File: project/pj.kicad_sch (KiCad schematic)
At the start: 15 parts, among them J1 RPi_GPIO, J10 Pico PWR enable, J2 2B+, J3 zero, J4 3A+, J5 3B+, J6 4, J7 Conn_01x02, J8 Conn_01x02, J9 External PWR, SW1 SW_Push, SW2 SW_Push

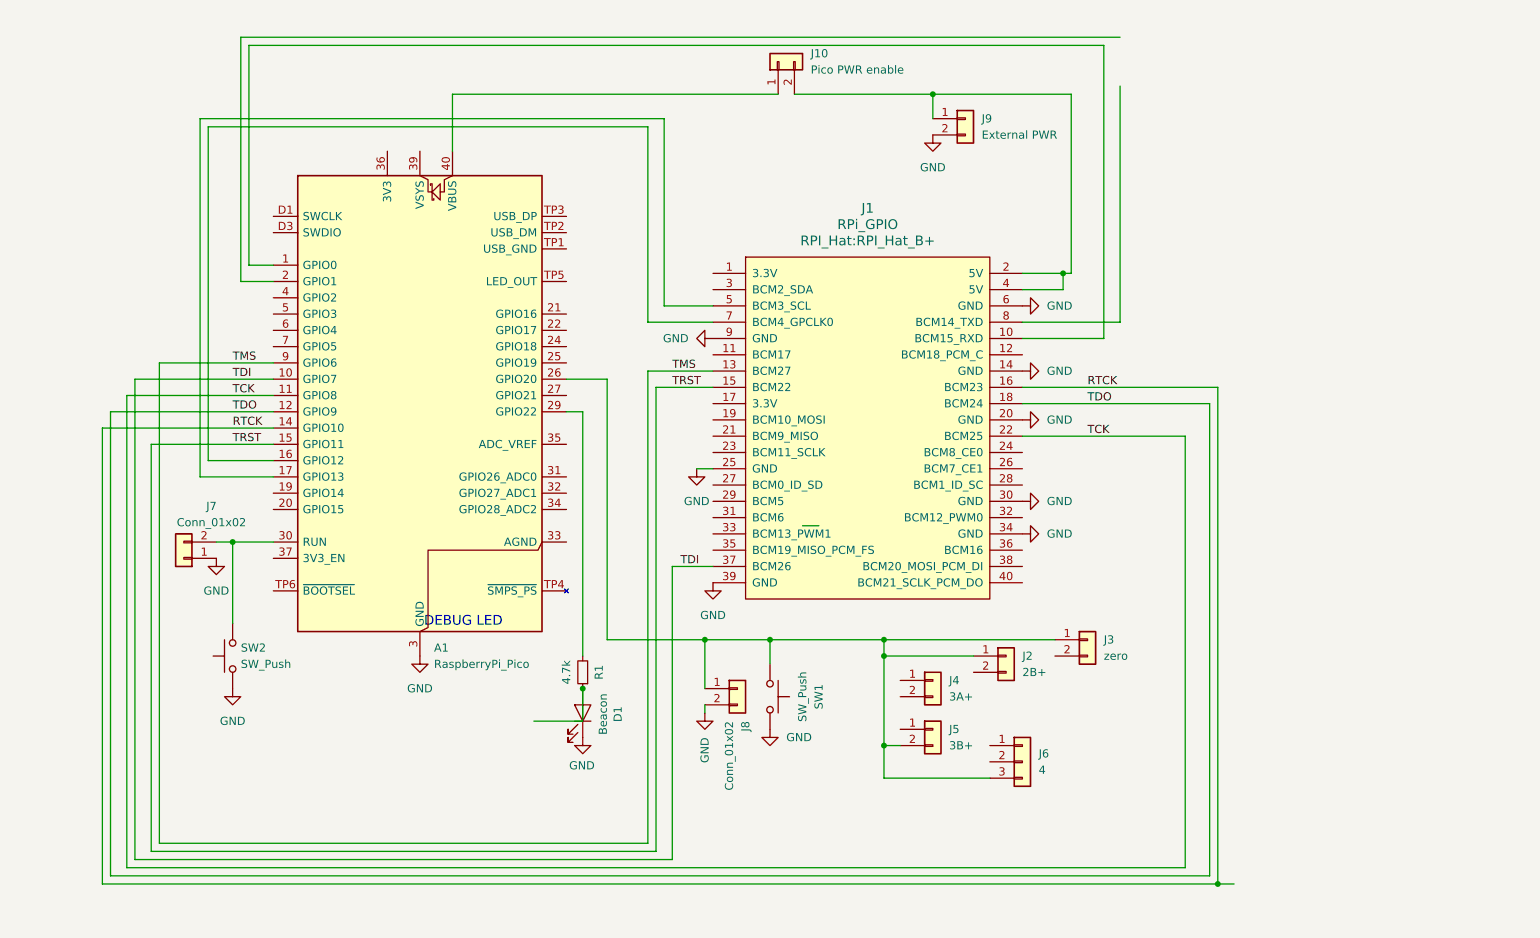
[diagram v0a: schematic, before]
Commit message: move reset over one, move reset headert to make room for row of holes.
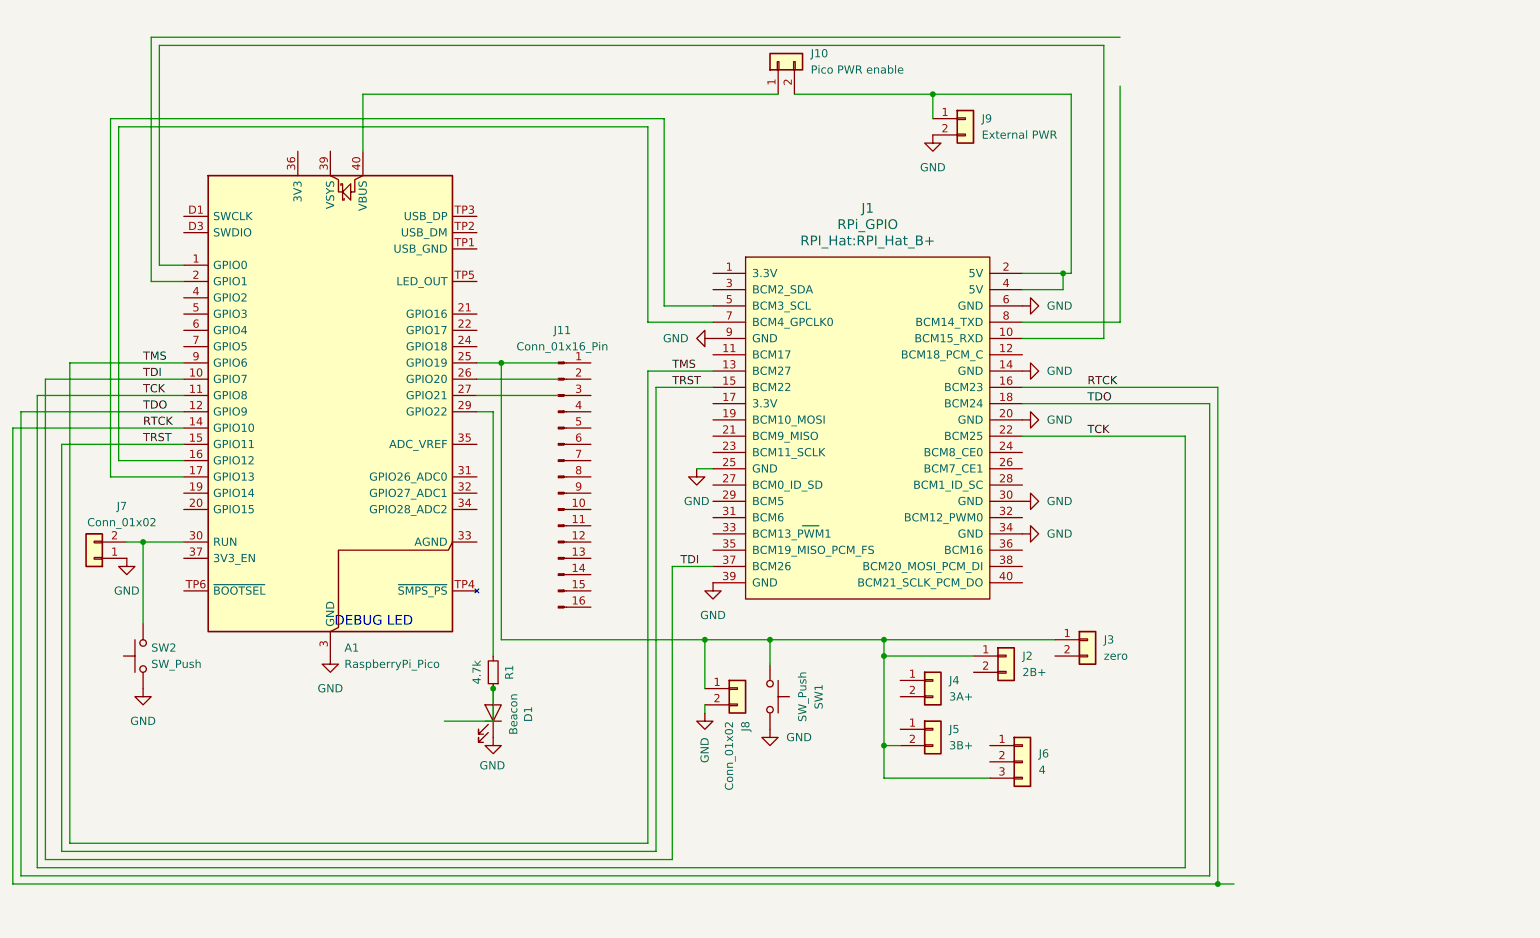
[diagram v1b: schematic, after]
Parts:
- added J11: Conn_01x16_Pin, symbol Connector:Conn_01x16_Pin
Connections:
- net at J2.1 (Pin_1), J3.1 (Pin_1), J5.2 (Pin_2)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: now also A1.25 (GPIO19); no longer A1.26 (GPIO20)
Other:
- moved on the sheet: A1, D1, J7, R1, SW2

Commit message: add 16 holes to put things in later.
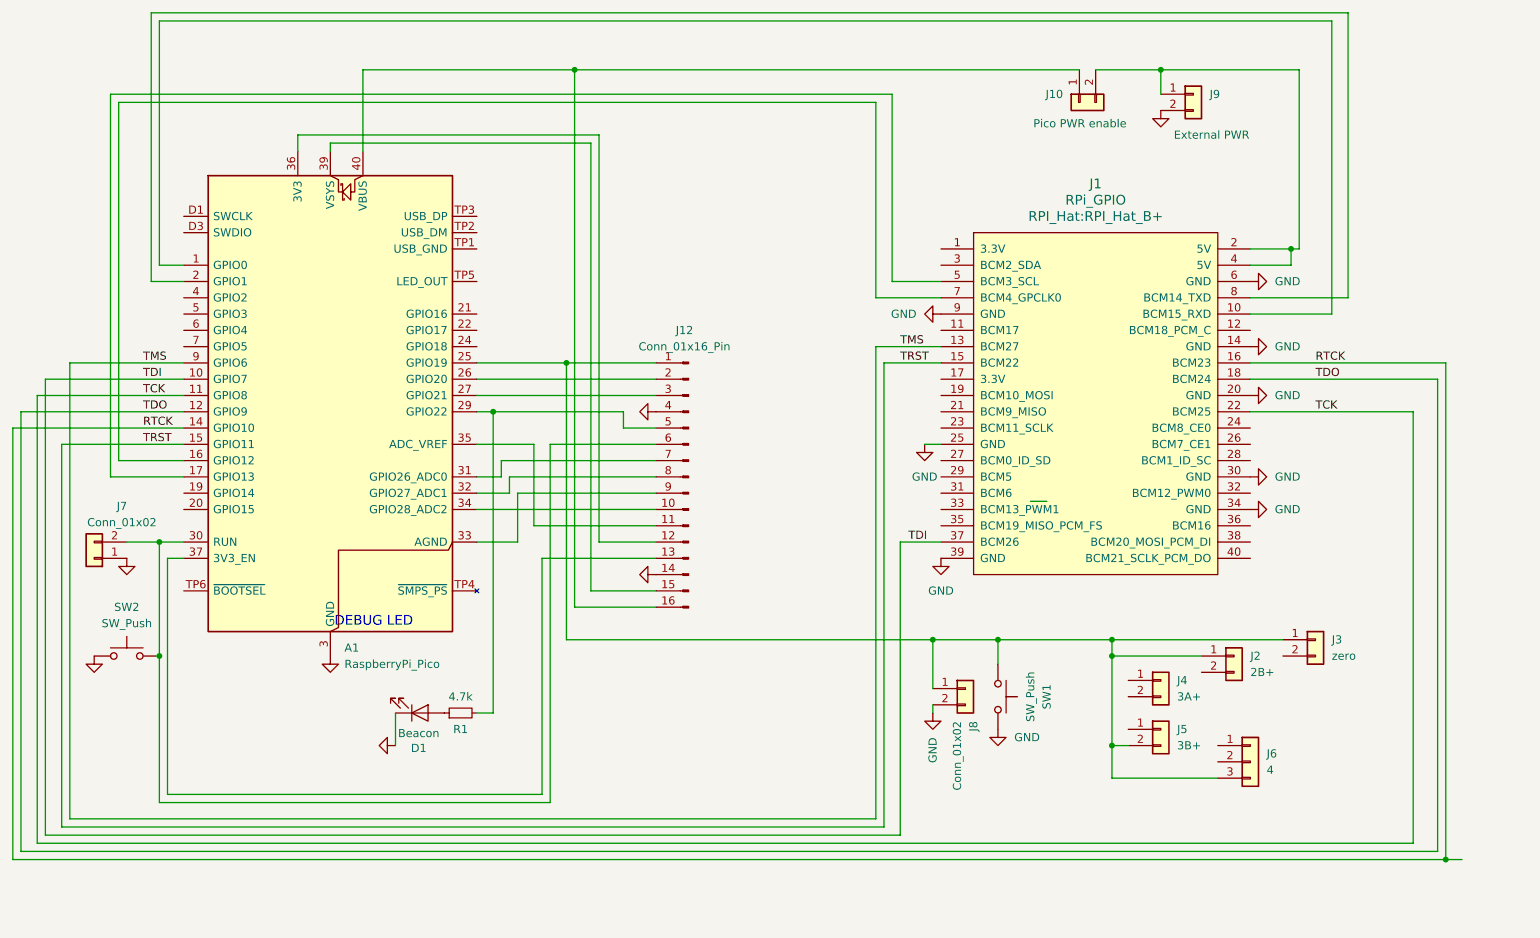
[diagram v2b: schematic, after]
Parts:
- removed J11: Conn_01x16_Pin, symbol Connector:Conn_01x16_Pin
- added J12: Conn_01x16_Pin, Connector_PinHeader_2.54mm:PinHeader_1x16_P2.54mm_Vertical, symbol Connector:Conn_01x16_Pin
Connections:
- net GND: now also J12.14 (Pin_14), J12.4 (Pin_4)
- net at A1.25 (GPIO19), J2.1 (Pin_1), J3.1 (Pin_1)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: now also J12.1 (Pin_1)
- net at A1.29 (GPIO22), R1.2: now also J12.5 (Pin_5)
- net at A1.30 (RUN), J7.2 (Pin_2), SW2.2: now also J12.6 (Pin_6)
- net at A1.2 (GPIO1): now also J1.8 (BCM14_TXD)
- net at A1.26 (GPIO20): now also J12.2 (Pin_2)
- net at A1.27 (GPIO21): now also J12.3 (Pin_3)
- net at A1.31 (GPIO26_ADC0): now also J12.7 (Pin_7)
- net at A1.32 (GPIO27_ADC1): now also J12.8 (Pin_8)
- net at A1.33 (AGND): now also J12.9 (Pin_9)
- net at A1.34 (GPIO28_ADC2): now also J12.10 (Pin_10)
- net at A1.35 (ADC_VREF): now also J12.11 (Pin_11)
- net at A1.36 (3V3): now also J12.12 (Pin_12)
- net at A1.37 (3V3_EN): now also J12.13 (Pin_13)
- net at A1.39 (VSYS): now also J12.15 (Pin_15)
- net at A1.40 (VBUS), J10.1 (Pin_1): now also J12.16 (Pin_16)
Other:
- moved on the sheet: D1, J1, J10, J2, J3, J4, J5, J6, J8, J9, R1, SW1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

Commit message: add missing connection to hole.
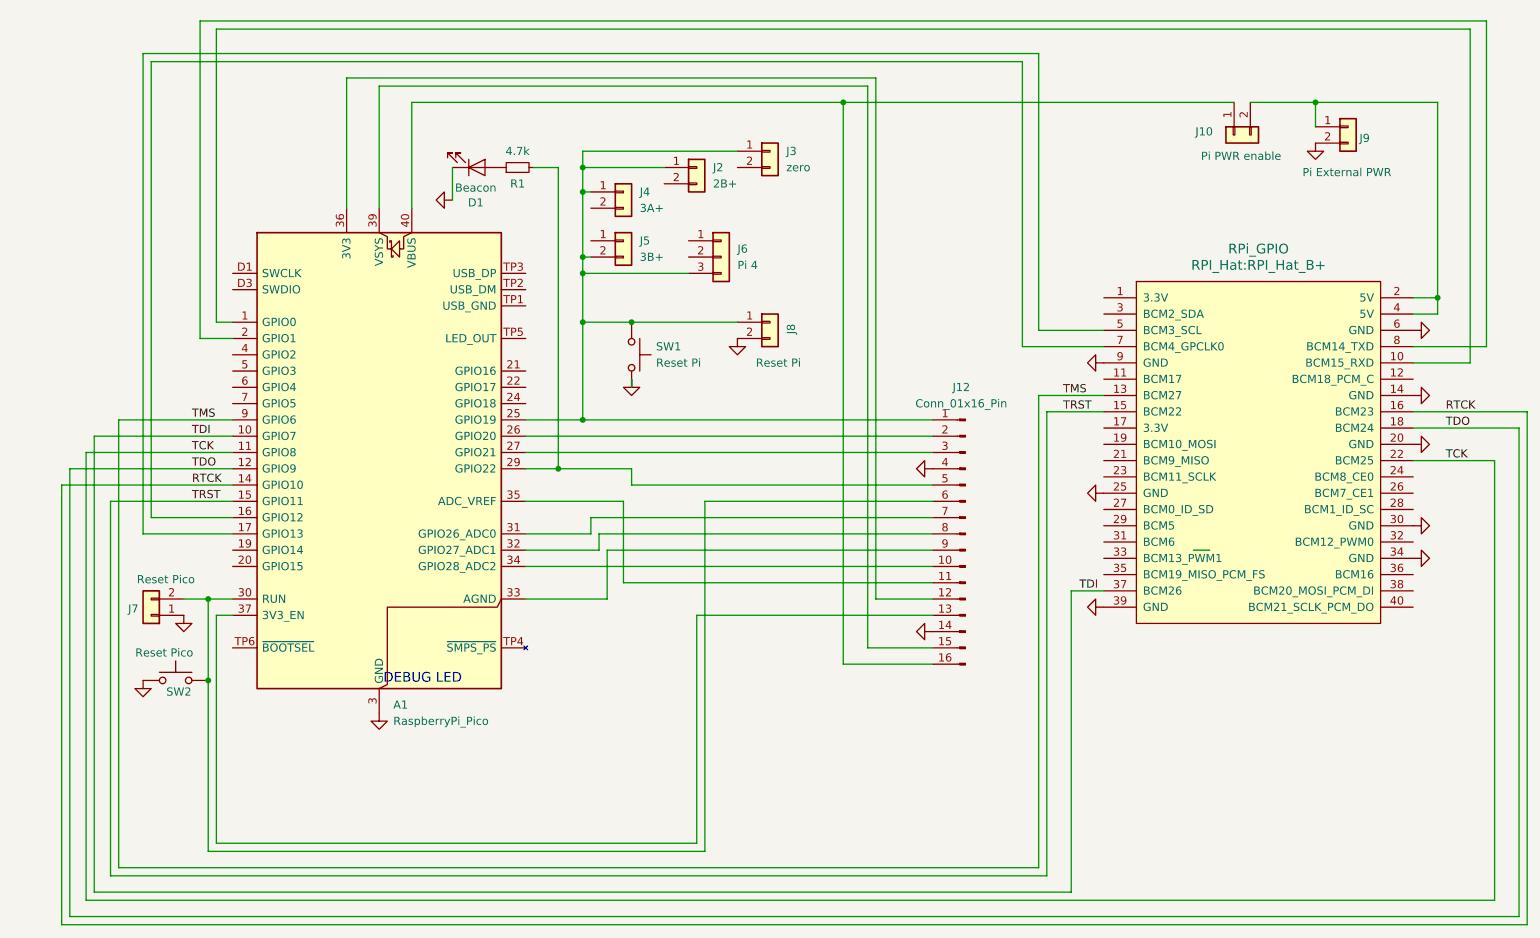
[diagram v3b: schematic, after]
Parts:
- J10: value Pico PWR enable -> Pi PWR enable
- J6: value 4 -> Pi 4
- J7: value Conn_01x02 -> Reset Pico
- J8: value Conn_01x02 -> Reset Pi
- J9: value External PWR -> Pi External PWR
- SW1: value SW_Push -> Reset Pi
- SW2: value SW_Push -> Reset Pico
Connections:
- net at A1.25 (GPIO19), J12.1 (Pin_1), J2.1 (Pin_1)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: now also J4.1 (Pin_1)
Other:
- moved on the sheet: A1, D1, J10, J12, J2, J3, J4, J5, J6, J7, J8, J9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

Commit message: 2.54 for all the headers.
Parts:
- J2, J3, J4, J5: footprint Connector_PinHeader_2.54mm:PinHeader_1x02_P2.54mm_Vertical -> Connector_PinSocket_2.54mm:PinSocket_1x02_P2.54mm_Vertical
- J6: footprint Connector_PinHeader_2.54mm:PinHeader_1x03_P2.54mm_Vertical -> Connector_PinSocket_2.54mm:PinSocket_1x03_P2.54mm_Vertical
- J7, J8, J9: footprint Connector_PinHeader_1.27mm:PinHeader_1x02_P1.27mm_Vertical -> Connector_PinHeader_2.54mm:PinHeader_1x02_P2.54mm_Vertical
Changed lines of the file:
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@@
 			)
 		)
-		(property "Footprint" "Connector_PinHeader_2.54mm:PinHeader_1x02_P2.54mm_Vertical"
+		(property "Footprint" "Connector_PinSocket_2.54mm:PinSocket_1x02_P2.54mm_Vertical"
 			(at 129.54 39.37 0)
 			(effects
@@
 			)
 		)
-		(property "Footprint" "Connector_PinHeader_2.54mm:PinHeader_1x02_P2.54mm_Vertical"
+		(property "Footprint" "Connector_PinSocket_2.54mm:PinSocket_1x02_P2.54mm_Vertical"
 			(at 118.11 43.18 0)
 			(effects
@@
 			)
 		)
-		(property "Footprint" "Connector_PinHeader_1.27mm:PinHeader_1x02_P1.27mm_Vertical"
+		(property "Footprint" "Connector_PinHeader_2.54mm:PinHeader_1x02_P2.54mm_Vertical"
 			(at 231.14 33.02 0)
 			(effects
@@
 			)
 		)
-		(property "Footprint" "Connector_PinHeader_1.27mm:PinHeader_1x02_P1.27mm_Vertical"
+		(property "Footprint" "Connector_PinHeader_2.54mm:PinHeader_1x02_P2.54mm_Vertical"
 			(at 140.97 63.5 0)
 			(effects
@@
 			)
 		)
-		(property "Footprint" "Connector_PinHeader_1.27mm:PinHeader_1x02_P1.27mm_Vertical"
+		(property "Footprint" "Connector_PinHeader_2.54mm:PinHeader_1x02_P2.54mm_Vertical"
 			(at 44.45 109.22 0)
 			(effects
@@
 			)
 		)
-		(property "Footprint" "Connector_PinHeader_2.54mm:PinHeader_1x03_P2.54mm_Vertical"
+		(property "Footprint" "Connector_PinSocket_2.54mm:PinSocket_1x03_P2.54mm_Vertical"
 			(at 133.35 53.34 0)
 			(effects
@@
 			)
 		)
-		(property "Footprint" "Connector_PinHeader_2.54mm:PinHeader_1x02_P2.54mm_Vertical"
+		(property "Footprint" "Connector_PinSocket_2.54mm:PinSocket_1x02_P2.54mm_Vertical"
 			(at 140.97 36.83 0)
 			(effects
@@
 			)
 		)
-		(property "Footprint" "Connector_PinHeader_2.54mm:PinHeader_1x02_P2.54mm_Vertical"
+		(property "Footprint" "Connector_PinSocket_2.54mm:PinSocket_1x02_P2.54mm_Vertical"
 			(at 118.11 50.8 0)
 			(effects

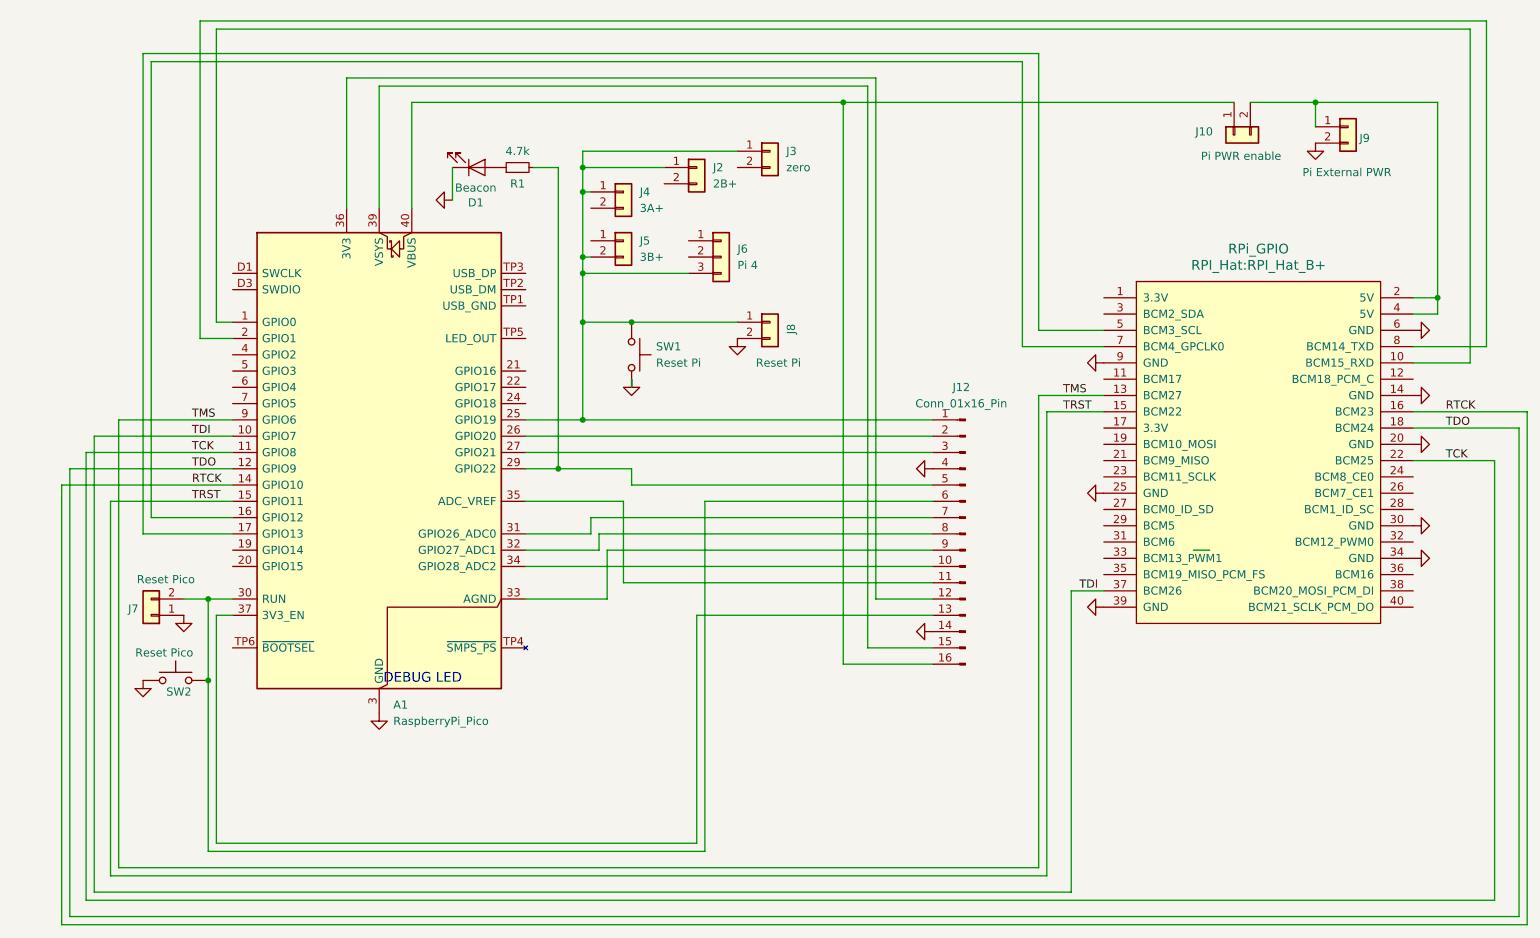
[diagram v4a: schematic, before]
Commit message: busses everywere.  with better labels.
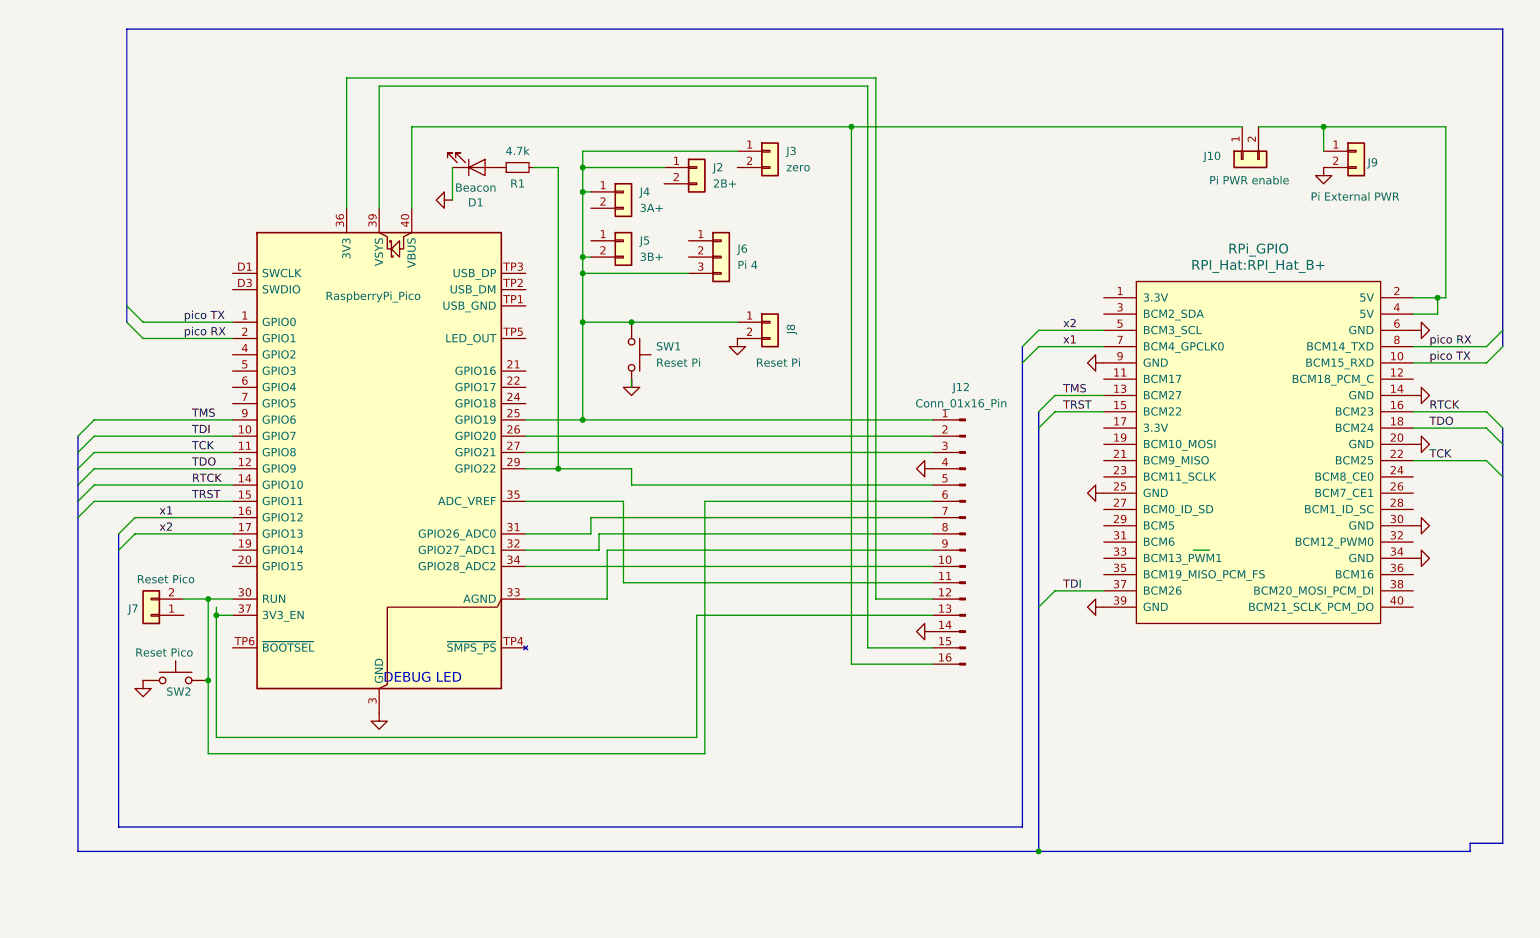
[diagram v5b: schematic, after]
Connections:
- net GND: no longer J7.1 (Pin_1)
- net pico TX: now reaches A1.1 (GPIO0), J1.10 (BCM15_RXD)
- net x1: now reaches A1.16 (GPIO12), J1.7 (BCM4_GPCLK0)
- net x2: now reaches A1.17 (GPIO13), J1.5 (BCM3_SCL)
- net pico RX: now reaches A1.2 (GPIO1), J1.8 (BCM14_TXD)
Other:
- moved on the sheet: J10, J9
